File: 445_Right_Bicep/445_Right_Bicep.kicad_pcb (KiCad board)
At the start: 2 copper layers, 60.1 x 48.6 mm, 0 parts

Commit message: Layout First Draft
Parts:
- added C11: 100nF, CL21F104ZAANNNC:CAPC2012X135N, F.Cu at (164.9, 97.0)
- added C12: 100nF, CL21F104ZAANNNC:CAPC2012X135N, F.Cu at (164.9, 102.1)
- added H1: MountingHole, MountingHole:MountingHole_2mm, F.Cu at (124.5, 51.7)
- added H2: MountingHole, MountingHole:MountingHole_2mm, F.Cu at (168.0, 51.7)
- added H3: MountingHole, MountingHole:MountingHole_2mm, F.Cu at (124.5, 118.0)
- added H4: MountingHole, MountingHole:MountingHole_2mm, F.Cu at (168.0, 118.0)
- added J10: 87583-2010RPLF, 87583-2010RPLF:AMPHENOL_87583-2010RPLF, F.Cu at (135.8, 97.2)
- added J12: 69167-107HLF, 69167-107HLF:AMPHENOL_69167-107HLF, F.Cu at (152.0, 114.7)
- added J5: 69167-107HLF, 69167-107HLF:AMPHENOL_69167-107HLF, F.Cu at (152.0, 105.4)
- added J8: SM02B-SRSS-TB_LF__SN_, SM02B-SRSS-TB_LF__SN_:SM02B-SRSS-TB_LF__SN_, F.Cu at (127.5, 69.3)
- added R2: 10k, RMCF0805JG10K0:RESC2012X65N, F.Cu at (164.9, 107.2)
- added U10: LP2950CZ-3.3_LFT3, LP2950CZ-3.3_LFT3:TO92127P521H735-3, F.Cu at (128.2, 82.3)
- added U13: TS3A5018D, TS3A5018D:SOIC127P600X175-16N, F.Cu at (152.1, 86.0)
- added U14: TS3A5018D, TS3A5018D:SOIC127P600X175-16N, F.Cu at (152.0, 95.8)
- added U2: ESP32-S3-WROOM-1-N16R8, ESP32-S3-WROOM-1-N16R8:XCVR_ESP32-S3-WROOM-1-N16R8, F.Cu at (151.3, 65.0)
- added U7: LSM6DSMTR, LSM6DSMTR (1):PQFN50P300X250X86-14N, F.Cu at (164.6, 93.2)
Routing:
- net +3.3V: track 0.00 -> 123.1 mm
- net INT1_3: track 0.00 -> 51.7 mm, vias 0 -> 1
- net INT1_2: track 0.00 -> 44.8 mm, vias 0 -> 2
- net INT1_1: track 0.00 -> 43.3 mm, vias 0 -> 1
- net SENSOR_3: track 0.00 -> 25.7 mm
- net D+: track 0.00 -> 24.9 mm, vias 0 -> 2
- net D-: track 0.00 -> 24.8 mm, vias 0 -> 2
- net SENSOR_1: track 0.00 -> 23.9 mm, vias 0 -> 2
- net MISO_3: track 0.00 -> 22.9 mm, vias 0 -> 1
- net MOSI_3: track 0.00 -> 22.7 mm, vias 0 -> 1
- net MOSI_1: track 0.00 -> 22.3 mm, vias 0 -> 1
- net MISO_1: track 0.00 -> 22.1 mm, vias 0 -> 1
- net MOSI_2: track 0.00 -> 21.1 mm, vias 0 -> 2
- net CLK3: track 0.00 -> 20.6 mm, vias 0 -> 1
- net MISO_2: track 0.00 -> 20.4 mm, vias 0 -> 2
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- added copper zone on F.Cu, net (none)
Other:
- board size 60.1 x 48.6 mm -> 48.6 x 71.4 mm
- board text added: "Right Bicep Version 1"

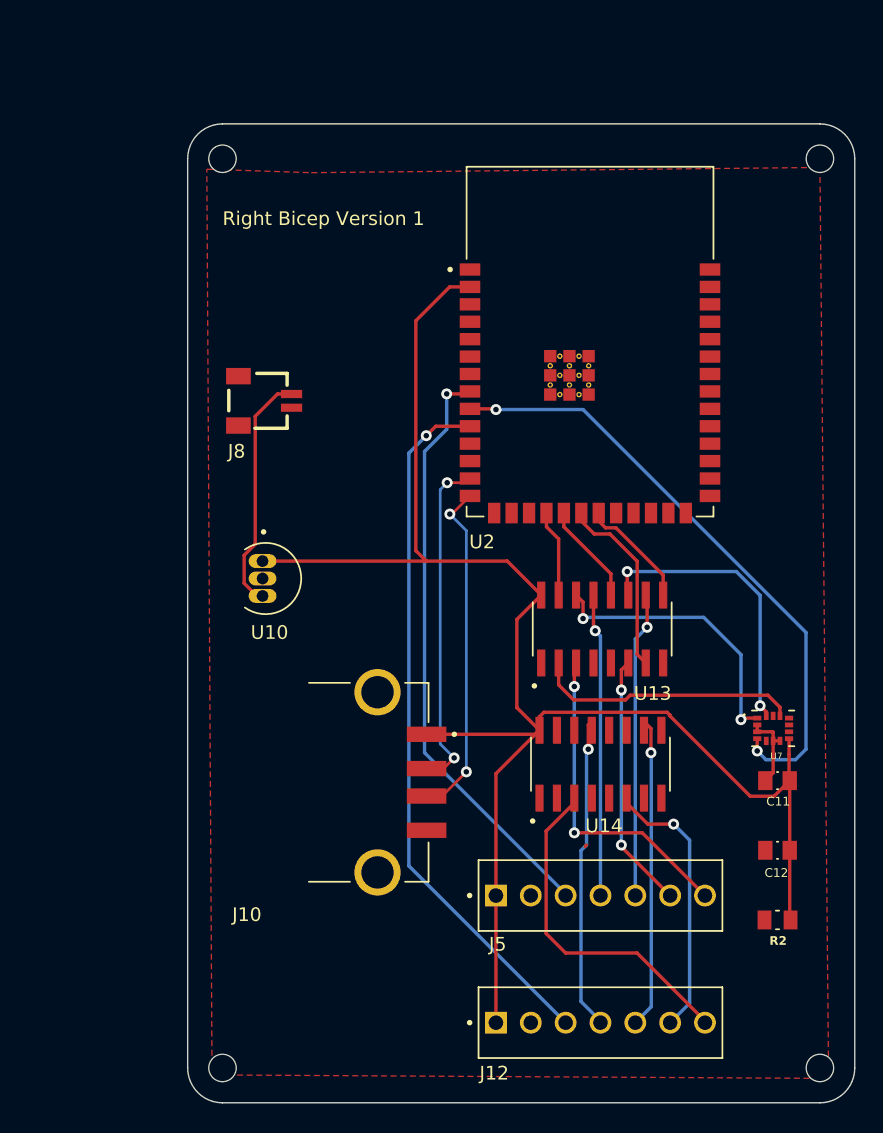
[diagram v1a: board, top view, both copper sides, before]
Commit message: adding buzzer
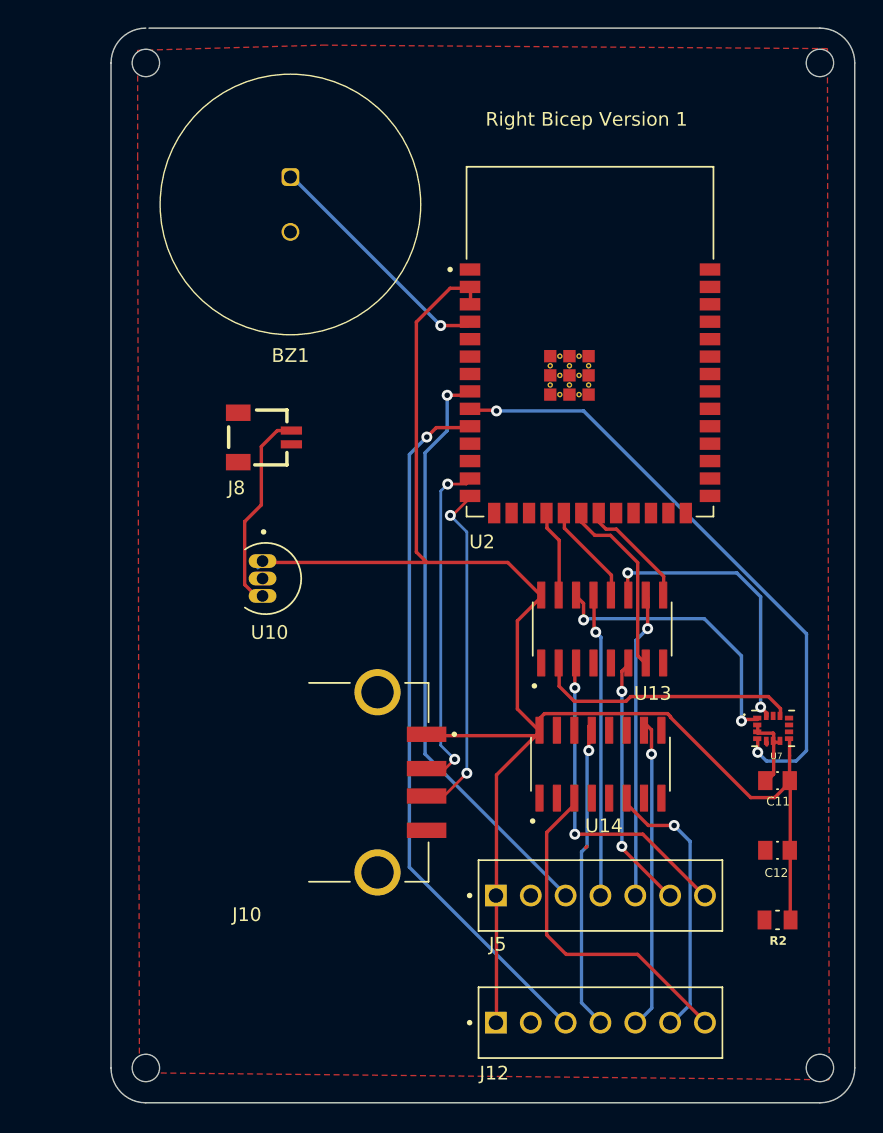
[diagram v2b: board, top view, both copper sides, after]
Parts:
- added BZ1: Buzzer, ECE 445 Footprints:AC-903-D-1P, F.Cu at (129.4, 55.0)
- moved H1 8.95 mm to (118.9, 44.7)
- moved H2 6.98 mm to (168.0, 44.7)
- moved H3 5.59 mm to (118.9, 118.0)
- moved J8 2.67 mm to (127.5, 72.0)
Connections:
- U2 pad 12: Net-(BZ1-+) -> unconnected-(U2-IO8-Pad12)
- U2 pad 4: unconnected-(U2-IO4-Pad4) -> Net-(BZ1-+)
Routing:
- net Net-(BZ1-+): track 0.00 -> 17.8 mm, vias 0 -> 1
- net Net-(U10-IN): track 17.6 -> 15.0 mm
- net +3.3V: track 123.1 -> 124.3 mm
- added copper zone on F.Cu, net GND
- removed copper zone on F.Cu, net (none)
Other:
- board size 48.6 x 71.4 mm -> 54.2 x 78.4 mm

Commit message: Edits 3/12
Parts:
- moved R2 49.9 mm to (135.4, 66.9), turned to -90 degrees
- moved J10 14.4 mm to (121.4, 96.6)
- moved C12 5.18 mm to (161.2, 98.6), turned to 180 degrees
- moved U7 4.03 mm to (160.8, 94.5)
- moved C11 1.93 mm to (166.1, 95.5), turned to 0 degrees
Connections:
- C11 pad 1: (no net) -> +3.3V
- C11 pad 2: (no net) -> GND
- C12 pad 1: (no net) -> GND
- C12 pad 2: (no net) -> +3.3V
- R2 pad 1: (no net) -> +3.3V
- R2 pad 2: (no net) -> GND
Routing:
- net CS2: track 0.00 -> 29.8 mm, vias 0 -> 2
- net SENSOR_SEL: track 0.00 -> 28.1 mm, vias 0 -> 3
- net MOSI: track 8.37 -> 22.8 mm, vias 0 -> 2
- net D+: track 24.9 -> 39.2 mm
- net D-: track 24.8 -> 39.0 mm
- net MISO: track 7.40 -> 21.1 mm, vias 0 -> 2
- net +3.3V: track 124.3 -> 137.0 mm, vias 0 -> 2
- net CLK2: track 0.00 -> 12.4 mm
- net CLK: track 13.5 -> 24.0 mm, vias 0 -> 2
- net CS1: track 6.35 -> 12.4 mm
- net INT1_2: track 44.8 -> 50.4 mm
- net CLK1: track 18.6 -> 22.8 mm
- net MOSI_2: track 21.1 -> 18.0 mm
- net MISO_2: track 20.4 -> 18.1 mm
- net SENSOR_2: track 19.3 -> 17.0 mm, vias 0 -> 2
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- added copper zone on B.Cu, net GND
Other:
- outline, holes or cut-outs redrawn

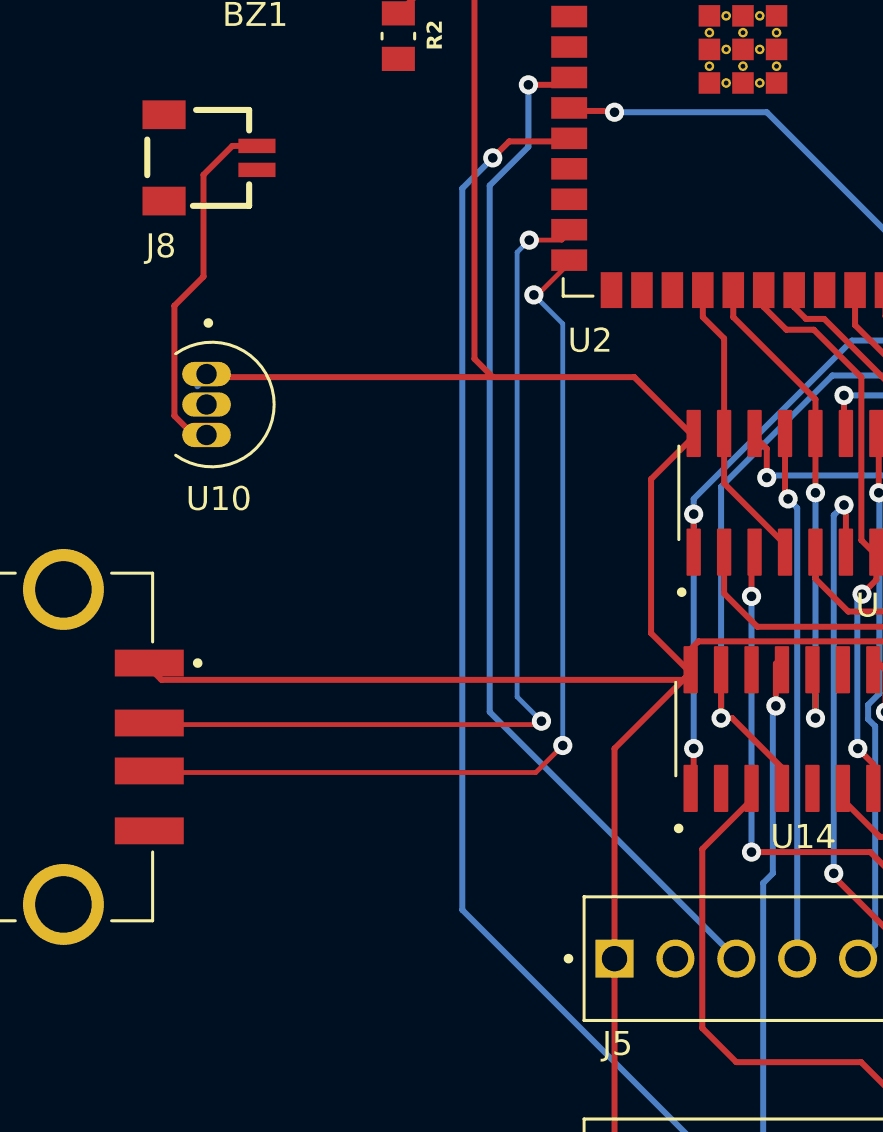
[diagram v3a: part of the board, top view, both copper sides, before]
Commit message: D+ and D- as differential pairs
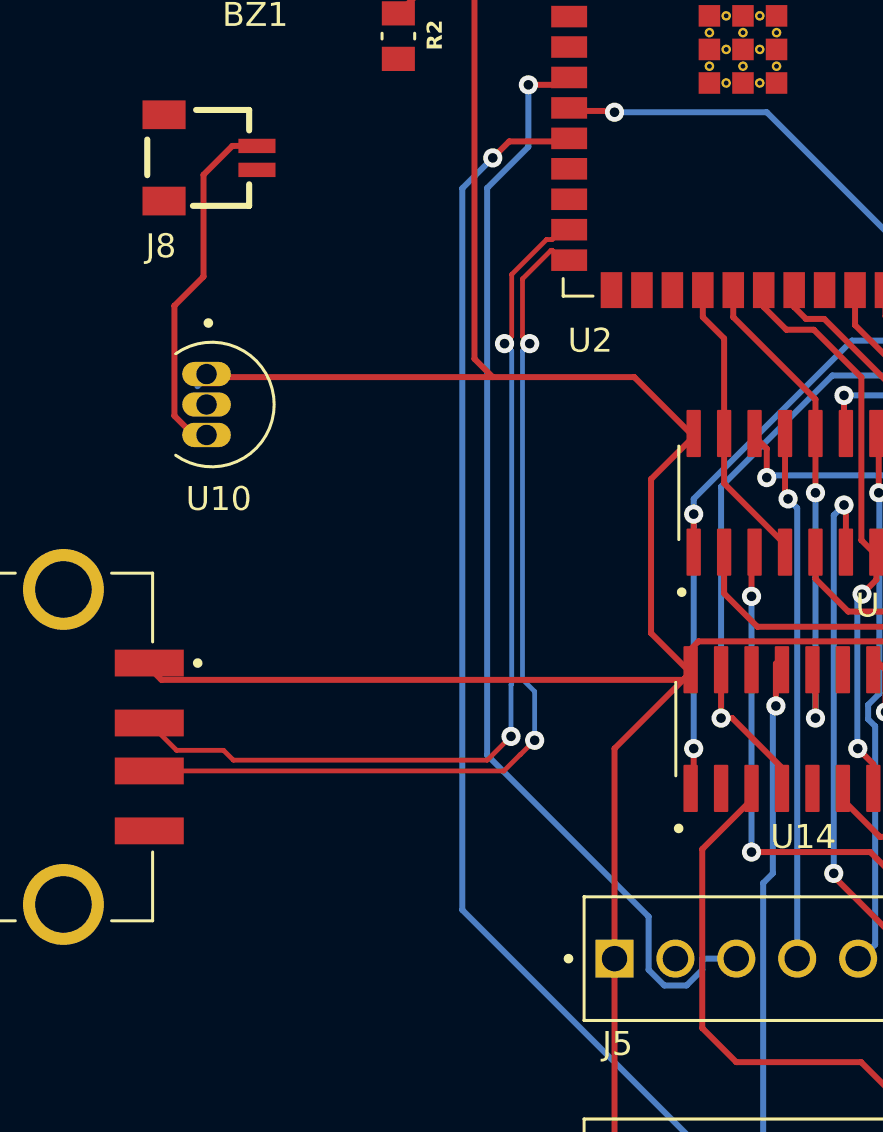
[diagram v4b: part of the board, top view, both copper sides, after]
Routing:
- net INT1_1: track 43.3 -> 47.0 mm
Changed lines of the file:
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@@
         (effects (font (size 1 1) (thickness 0.15)))
     )
-    (fp_text user "PCB EDGE" (at 9 4.5 90) (layer "F.Fab")
+    (fp_text user "PCB EDGE" (at 9 4.5 90) (layer "F.Fab") hide
         (effects (font (size 1 1) (thickness 0.15)))
     )
@@
   (segment (start 142.327 68.961) (end 142.507 68.781) (width 0.25) (layer "F.Cu") (net 3))
   (via (at 140.806 68.961) (size 0.8) (drill 0.4) (layers "F.Cu" "B.Cu") (net 3))
-  (segment (start 149.479 105.41) (end 139.192 95.123) (width 0.25) (layer "B.Cu") (net 3))
-  (segment (start 139.192 95.123) (end 139.192 73.161305) (width 0.25) (layer "B.Cu") (net 3))
+  (segment (start 148.059 105.41) (end 148.059 105.87392) (width 0.25) (layer "B.Cu") (net 3))
+  (segment (start 145.819 105.87392) (end 145.819 103.655) (width 0.25) (layer "B.Cu") (net 3))
+  (segment (start 149.479 105.41) (end 148.059 105.41) (width 0.25) (layer "B.Cu") (net 3))
+  (segment (start 139.085 73.268305) (end 140.806 71.547305) (width 0.25) (layer "B.Cu") (net 3))
+  (segment (start 147.40292 106.53) (end 146.47508 106.53) (width 0.25) (layer "B.Cu") (net 3))
+  (segment (start 146.47508 106.53) (end 145.819 105.87392) (width 0.25) (layer "B.Cu") (net 3))
+  (segment (start 148.059 105.87392) (end 147.40292 106.53) (width 0.25) (layer "B.Cu") (net 3))
+  (segment (start 145.819 103.655) (end 139.085 96.921) (width 0.25) (layer "B.Cu") (net 3))
   (segment (start 140.806 71.547305) (end 140.806 68.961) (width 0.25) (layer "B.Cu") (net 3))
-  (segment (start 139.192 73.161305) (end 140.806 71.547305) (width 0.25) (layer "B.Cu") (net 3))
+  (segment (start 139.085 96.921) (end 139.085 73.268305) (width 0.25) (layer "B.Cu") (net 3))
   (segment (start 149.479 105.537) (end 149.479 105.41) (width 0.25) (layer "B.Cu") (net 3))
   (segment (start 151.638 86.233) (end 151.511 86.106) (width 0.25) (layer "F.Cu") (net 4))
@@
   (via (at 150.114 90.297) (size 0.8) (drill 0.4) (layers "F.Cu" "B.Cu") (net 7))
   (segment (start 150.114 100.965) (end 150.114 90.297) (width 0.25) (layer "B.Cu") (net 7))
-  (segment (start 124.865 95.647) (end 141.208 95.647) (width 0.2) (layer "F.Cu") (net 8))
-  (segment (start 140.843 75.438) (end 142.2 75.438) (width 0.2) (layer "F.Cu") (net 8))
-  (segment (start 142.2 75.438) (end 142.507 75.131) (width 0.2) (layer "F.Cu") (net 8))
-  (segment (start 141.208 95.647) (end 141.351 95.504) (width 0.2) (layer "F.Cu") (net 8))
-  (via (at 140.843 75.438) (size 0.8) (drill 0.4) (layers "F.Cu" "B.Cu") (net 8))
-  (via (at 141.351 95.504) (size 0.8) (drill 0.4) (layers "F.Cu" "B.Cu") (net 8))
-  (segment (start 140.335 94.488) (end 140.335 75.946) (width 0.2) (layer "B.Cu") (net 8))
-  (segment (start 140.335 75.946) (end 140.843 75.438) (width 0.2) (layer "B.Cu") (net 8))
-  (segment (start 141.351 95.504) (end 140.335 94.488) (width 0.2) (layer "B.Cu") (net 8))
-  (segment (start 141.184 77.724) (end 142.507 76.401) (width 0.2) (layer "F.Cu") (net 9))
-  (segment (start 141.113 97.647) (end 142.24 96.52) (width 0.2) (layer "F.Cu") (net 9))
-  (segment (start 124.865 97.647) (end 141.113 97.647) (width 0.2) (layer "F.Cu") (net 9))
-  (segment (start 141.035 77.724) (end 141.184 77.724) (width 0.2) (layer "F.Cu") (net 9))
-  (via (at 142.24 96.52) (size 0.8) (drill 0.4) (layers "F.Cu" "B.Cu") (net 9))
-  (via (at 141.035 77.724) (size 0.8) (drill 0.4) (layers "F.Cu" "B.Cu") (net 9))
-  (segment (start 142.24 96.52) (end 142.24 78.929) (width 0.2) (layer "B.Cu") (net 9))
-  (segment (start 142.24 78.929) (end 141.035 77.724) (width 0.2) (layer "B.Cu") (net 9))
+  (segment (start 141.5648 75.414) (end 140.109999 76.868801) (width 0.2) (layer "F.Cu") (net 8))
+  (segment (start 126.132 96.72075) (end 124.992 95.58075) (width 0.2) (layer "F.Cu") (net 8))
+  (segment (start 142.207 75.004) (end 141.797 75.414) (width 0.2) (layer "F.Cu") (net 8))
+  (segment (start 140.109999 76.868801) (end 140.109999 79.456001) (width 0.2) (layer "F.Cu") (net 8))
+  (segment (start 128.08975 96.72075) (end 126.132 96.72075) (width 0.2) (layer "F.Cu") (net 8))
+  (segment (start 139.089251 97.130749) (end 128.499749 97.130749) (width 0.2) (layer "F.Cu") (net 8))
+  (segment (start 128.499749 97.130749) (end 128.08975 96.72075) (width 0.2) (layer "F.Cu") (net 8))
+  (segment (start 141.797 75.414) (end 141.5648 75.414) (width 0.2) (layer "F.Cu") (net 8))
+  (segment (start 140.081 96.139) (end 139.089251 97.130749) (width 0.2) (layer "F.Cu") (net 8))
+  (segment (start 140.109999 79.456001) (end 139.81 79.756) (width 0.2) (layer "F.Cu") (net 8))
+  (segment (start 142.507 75.004) (end 142.207 75.004) (width 0.2) (layer "F.Cu") (net 8))
+  (via (at 139.81 79.756) (size 0.8) (drill 0.4) (layers "F.Cu" "B.Cu") (net 8))
+  (via (at 140.081 96.139) (size 0.8) (drill 0.4) (layers "F.Cu" "B.Cu") (net 8))
+  (segment (start 140.109999 93.946198) (end 140.109999 80.055999) (width 0.2) (layer "B.Cu") (net 8))
+  (segment (start 140.081 93.975197) (end 140.109999 93.946198) (width 0.2) (layer "B.Cu") (net 8))
+  (segment (start 140.081 96.139) (end 140.081 93.975197) (width 0.2) (layer "B.Cu") (net 8))
+  (segment (start 140.109999 80.055999) (end 139.81 79.756) (width 0.2) (layer "B.Cu") (net 8))
+  (segment (start 140.560001 77.055199) (end 140.560001 79.456001) (width 0.2) (layer "F.Cu") (net 9))
+  (segment (start 139.78225 97.58075) (end 124.992 97.58075) (width 0.2) (layer "F.Cu") (net 9))
+  (segment (start 141.7512 75.864) (end 140.560001 77.055199) (width 0.2) (layer "F.Cu") (net 9))
+  (segment (start 140.560001 79.456001) (end 140.86 79.756) (width 0.2) (layer "F.Cu") (net 9))
+  (segment (start 140.462 96.901) (end 139.78225 97.58075) (width 0.2) (layer "F.Cu") (net 9))
+  (segment (start 141.067396 96.3034) (end 140.469796 96.901) (width 0.2) (layer "F.Cu") (net 9))
+  (segment (start 141.797 75.864) (end 141.7512 75.864) (width 0.2) (layer "F.Cu") (net 9))
+  (segment (start 142.207 76.274) (end 141.797 75.864) (width 0.2) (layer "F.Cu") (net 9))
+  (segment (start 140.469796 96.901) (end 140.462 96.901) (width 0.2) (layer "F.Cu") (net 9))
+  (segment (start 142.507 76.274) (end 142.207 76.274) (width 0.2) (layer "F.Cu") (net 9))
+  (via (at 140.86 79.756) (size 0.8) (drill 0.4) (layers "F.Cu" "B.Cu") (net 9))
+  (via (at 141.067396 96.3034) (size 0.8) (drill 0.4) (layers "F.Cu" "B.Cu") (net 9))
+  (segment (start 140.560001 93.759802) (end 140.560001 80.055999) (width 0.2) (layer "B.Cu") (net 9))
+  (segment (start 140.560001 80.055999) (end 140.86 79.756) (width 0.2) (layer "B.Cu") (net 9))
+  (segment (start 141.067396 94.267197) (end 140.560001 93.759802) (width 0.2) (layer "B.Cu") (net 9))
+  (segment (start 141.067396 96.3034) (end 141.067396 94.267197) (width 0.2) (layer "B.Cu") (net 9))
   (segment (start 140.007 71.321) (end 142.507 71.321) (width 0.25) (layer "F.Cu") (net 10))
   (segment (start 149.479 114.554) (end 149.352 114.427) (width 0.25) (layer "F.Cu") (net 10))
